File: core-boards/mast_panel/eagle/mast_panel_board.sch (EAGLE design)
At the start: 28 parts, among them J1 2-PIN_2MM-V, J4 4-PIN_2MM-H, U1 ATMEGA328P-AUR, U3 MCP2551T-I/SN

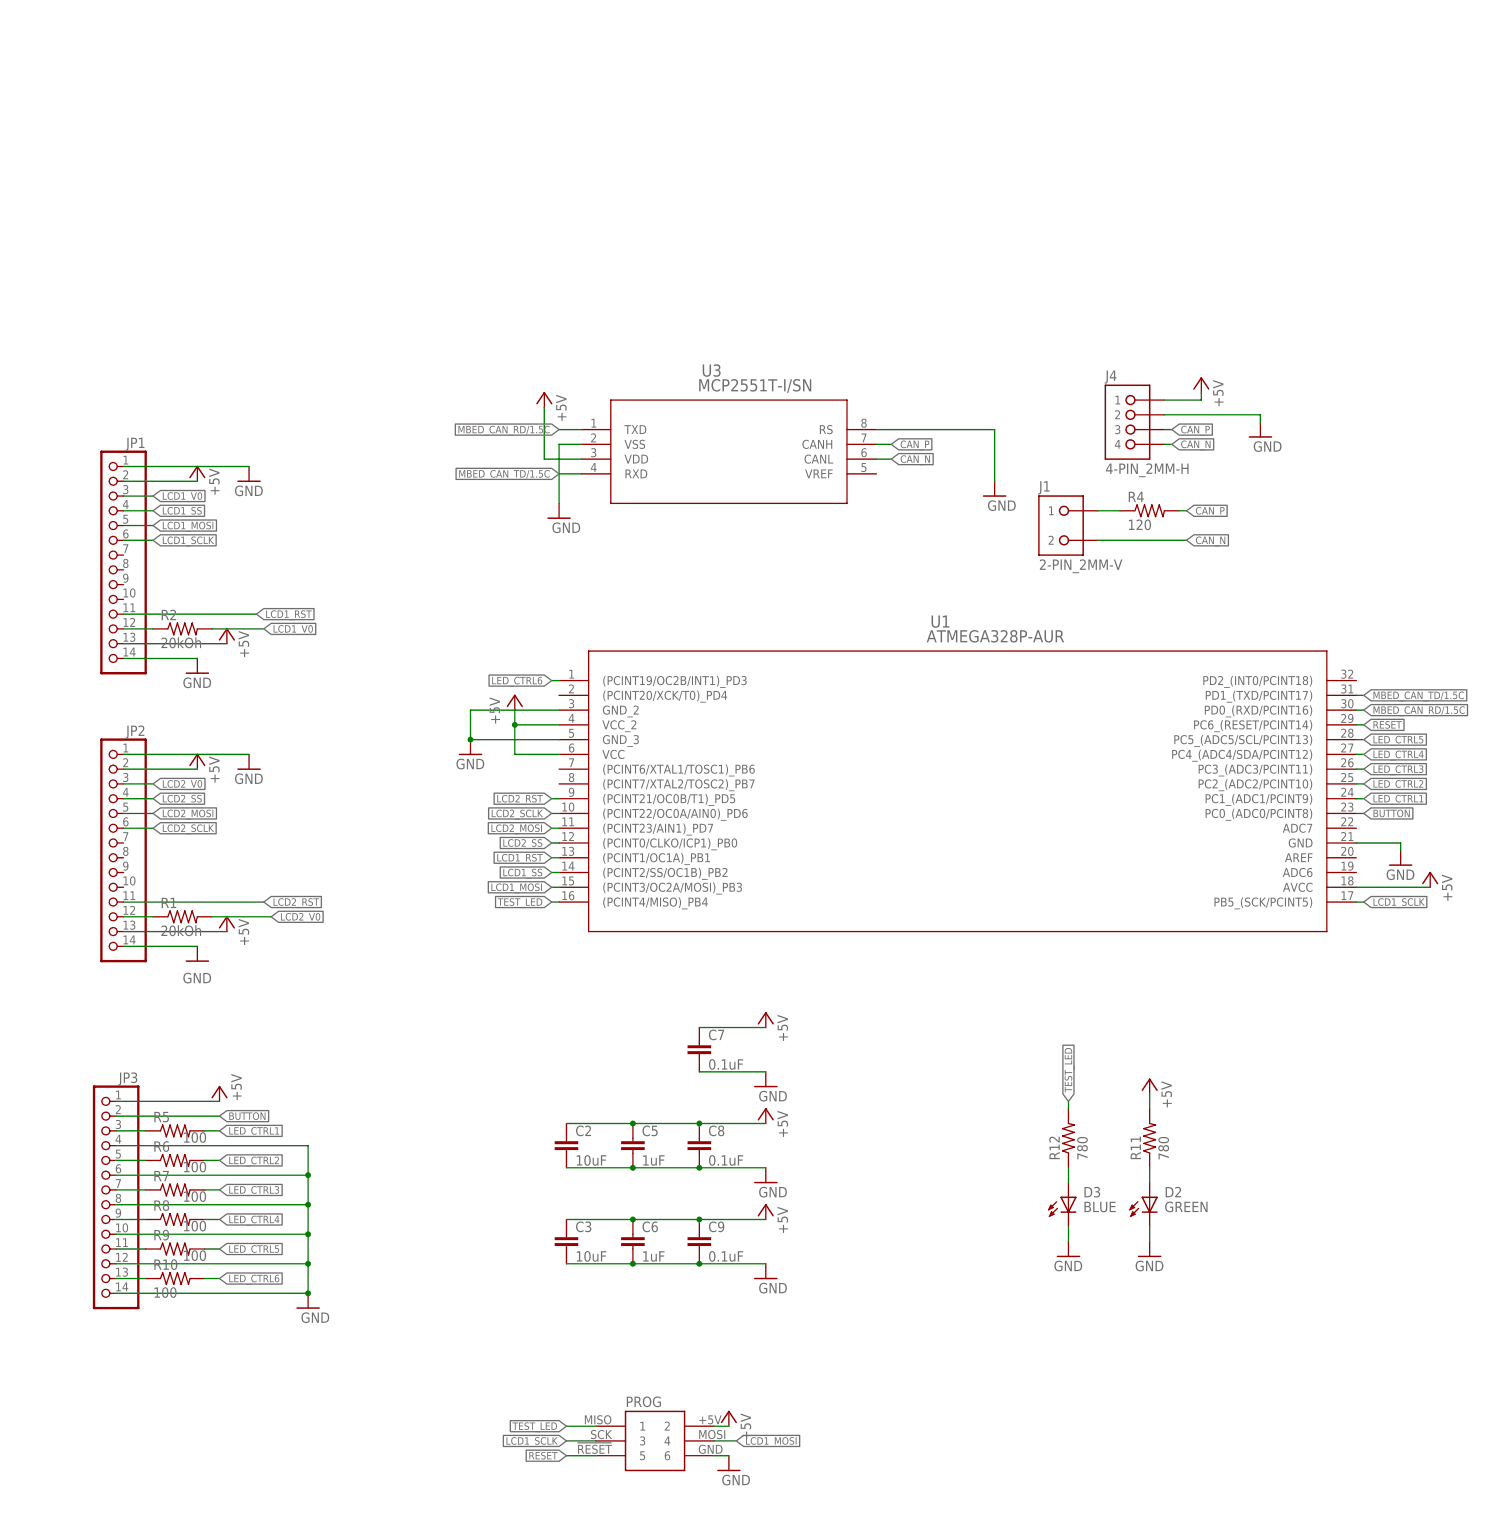
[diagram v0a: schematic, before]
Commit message: 2/16/20
Cleaned up some things, added surface mount reset button
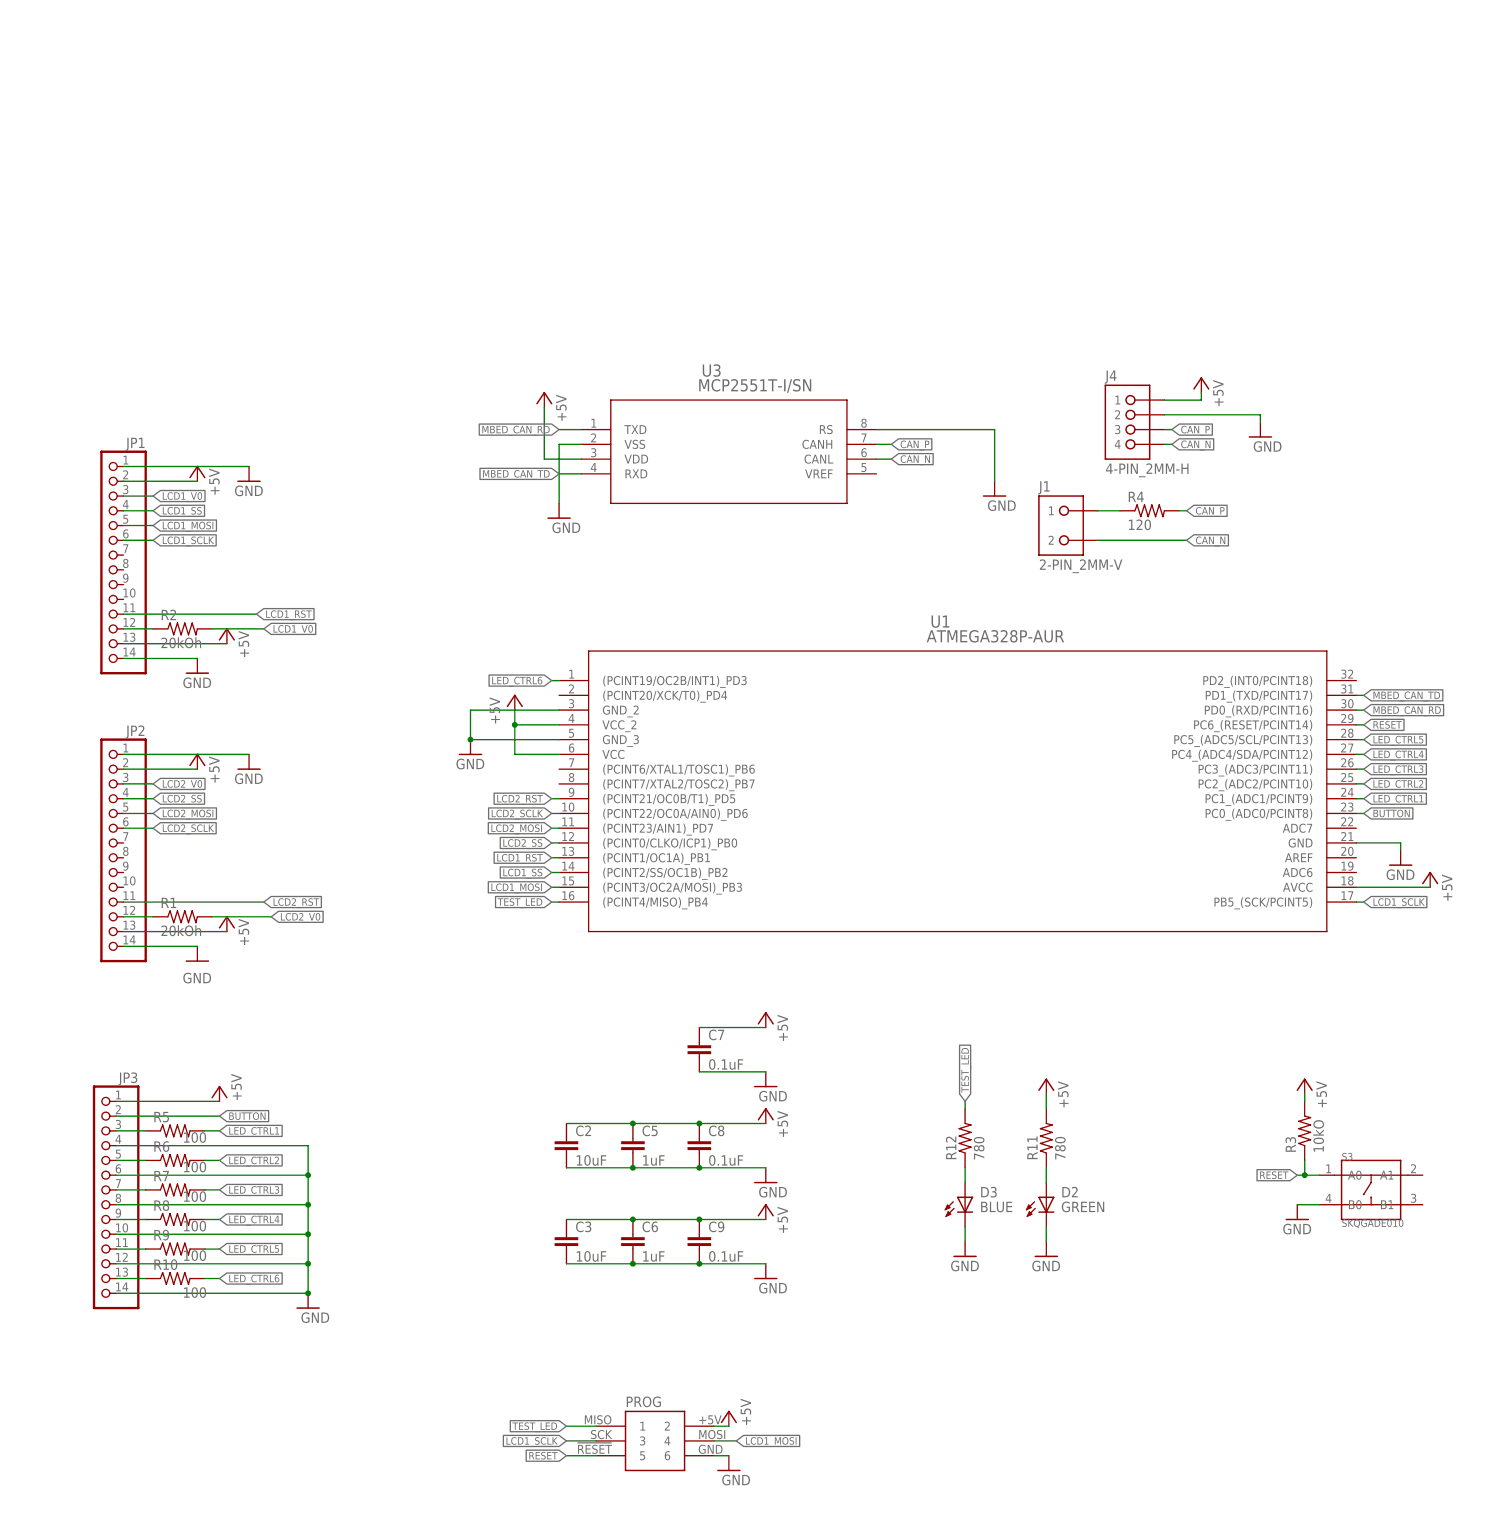
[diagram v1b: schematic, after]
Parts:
- added R3: 10kO, rcl:R-US_R0603
- added S3: SKQGADE010, rgb-led:SMD-SWITCH-TOP-260GF(4P-D5.2MM)
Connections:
- net MBED_CAN_RD/1.5C renamed MBED_CAN_RD
- net MBED_CAN_TD/1.5C renamed MBED_CAN_TD
- net +5V: now also R3.2
- net GND: now also S3.B0
- net RESET: now also R3.1, S3.A0
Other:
- note added: "Decoupling Capacitors"
- note added: "ICSP"
- note added: "Reset Button"
- note removed: "Decoupling Capacitor"
- moved on the sheet: D2, D3, R11, R12
